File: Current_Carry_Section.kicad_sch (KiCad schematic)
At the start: 4 parts, among them U3_1 TPS259620DDAR, U3_2 TPS259620DDAR, U3_3 TPS259620DDAR, U3_4 TPS259620DDAR

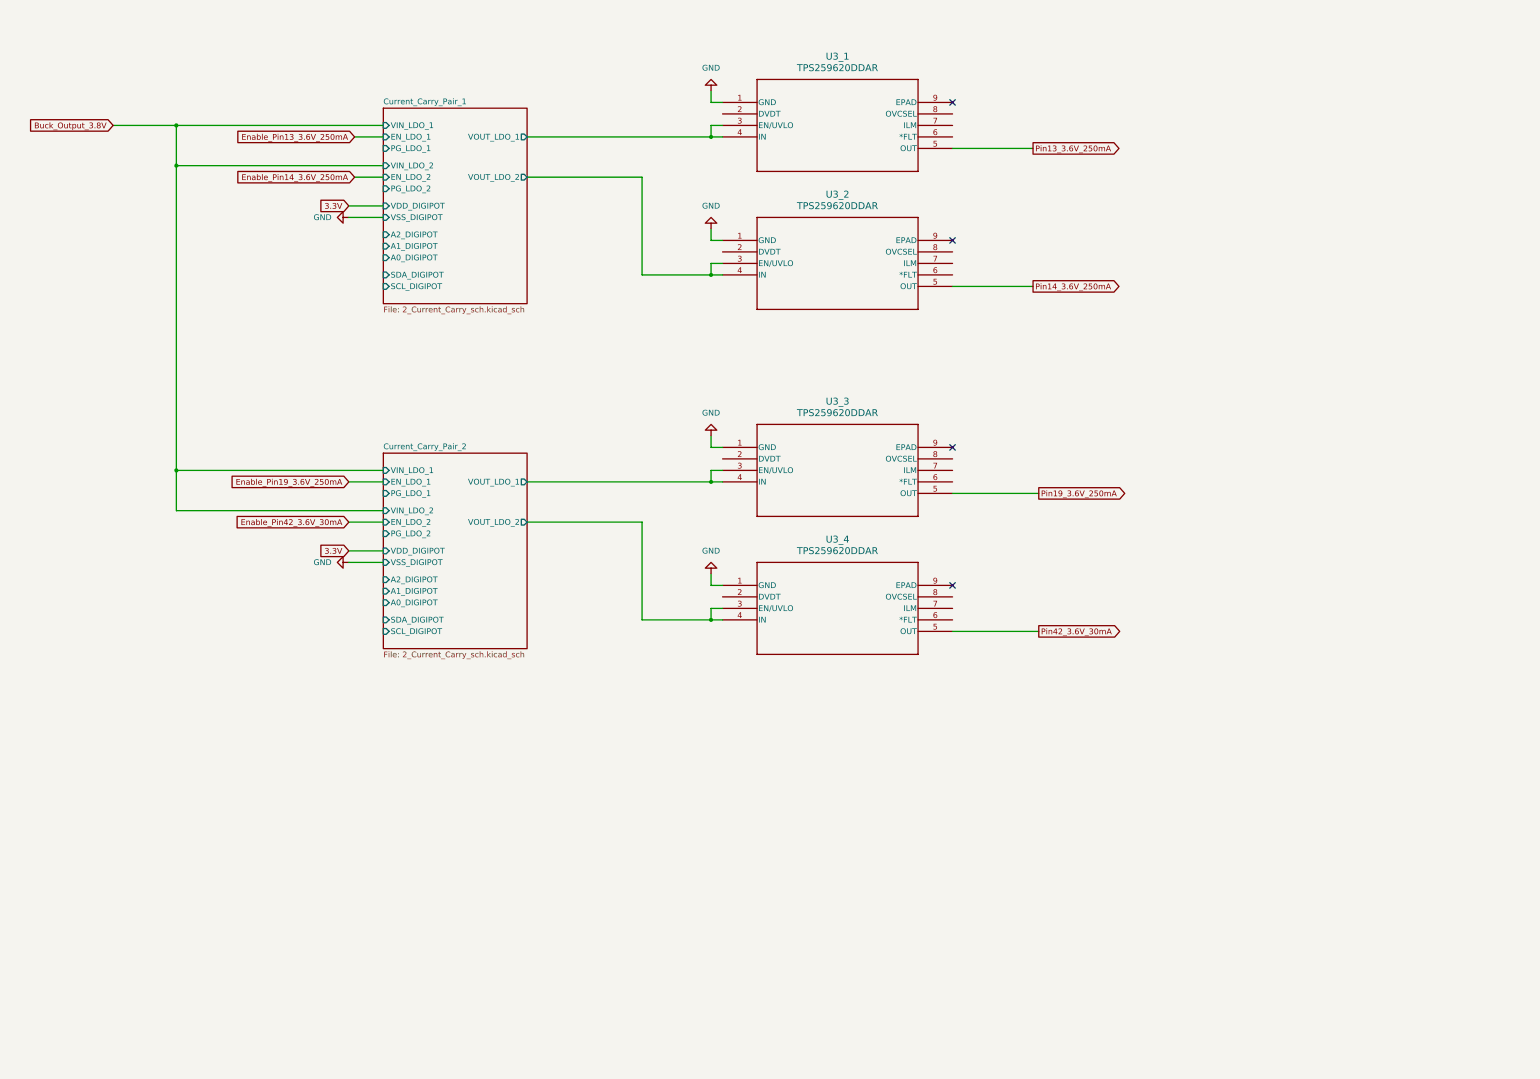
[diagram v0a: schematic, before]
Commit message: Full schematic connection without ratio consideration.
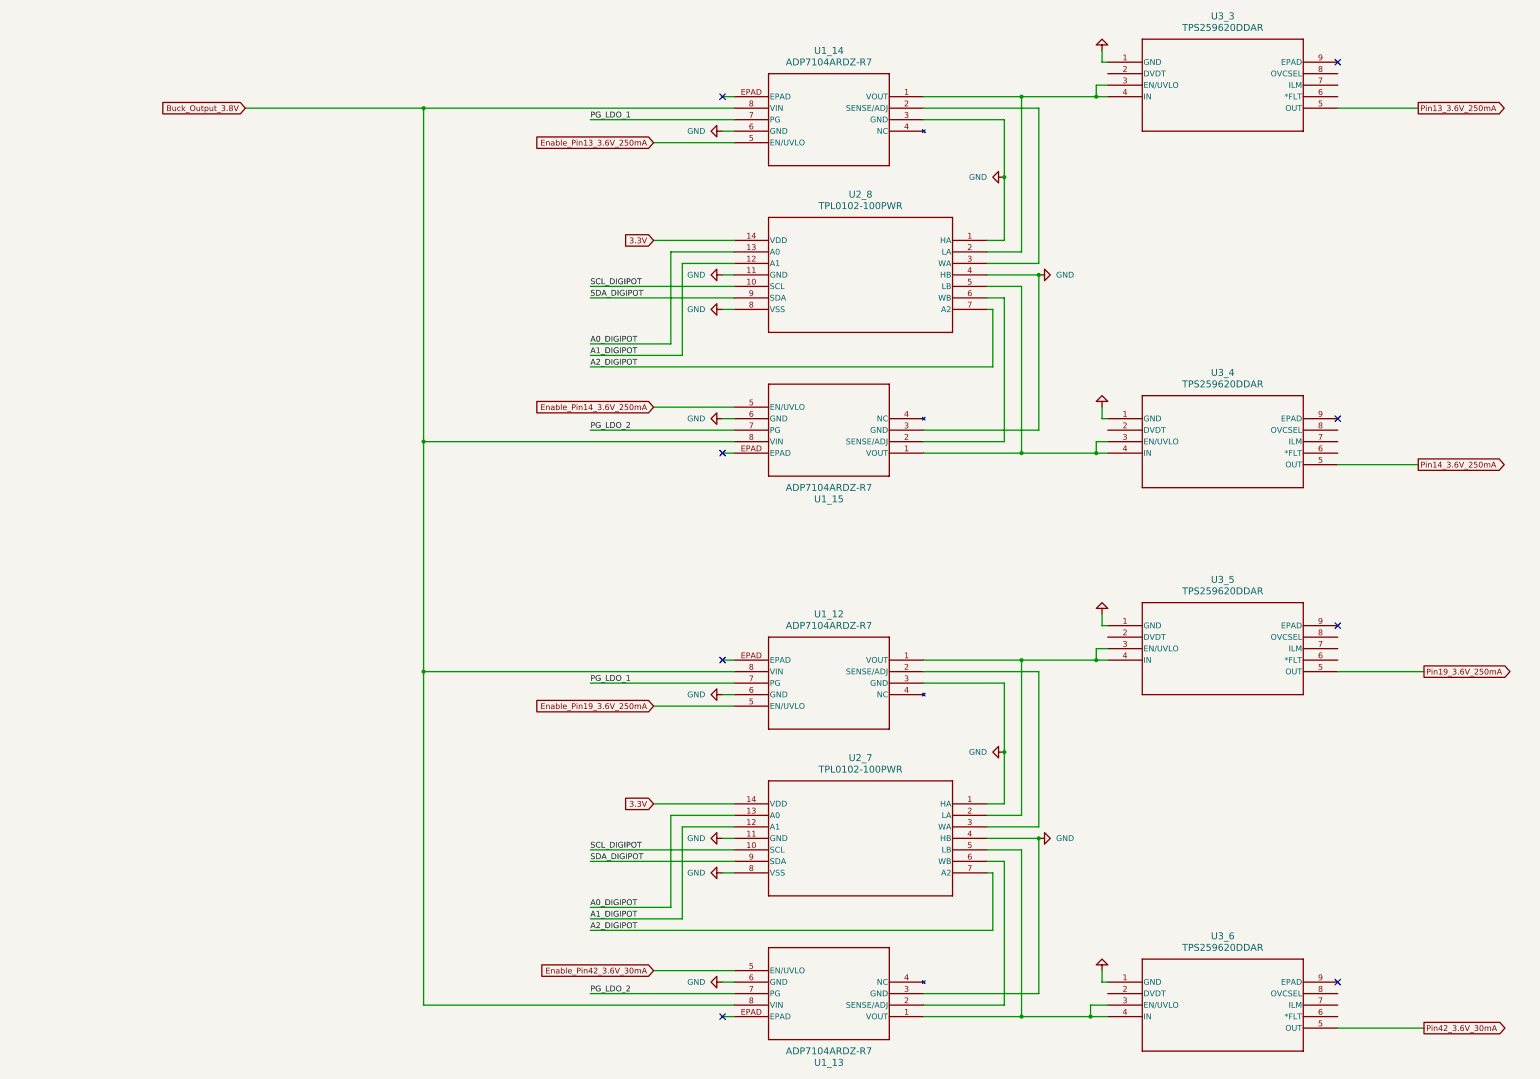
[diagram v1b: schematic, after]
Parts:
- added U1_12, U1_13, U1_14, U1_15: ADP7104ARDZ-R7, RD_8_2_ADI, symbol Adjustable Low-Dropout Regulator:ADP7104ARDZ-R7
- added U2_7, U2_8: TPL0102-100PWR, PW14, symbol Digital Potentiometer:TPL0102-100PWR
- renumbered U3_1 to U3_3, U3_2 to U3_4, U3_3 to U3_5, U3_4 to U3_6
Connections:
- net 3.3V: now also U2_7.14 (VDD), U2_8.14 (VDD)
- net Buck_Output_3.8V: now also U1_12.8 (VIN), U1_13.8 (VIN), U1_14.8 (VIN), U1_15.8 (VIN)
- net Enable_Pin13_3.6V_250mA: now also U1_14.5 (EN/UVLO)
- net Enable_Pin14_3.6V_250mA: now also U1_15.5 (EN/UVLO)
- net Enable_Pin19_3.6V_250mA: now also U1_12.5 (EN/UVLO)
- net Enable_Pin42_3.6V_30mA: now also U1_13.5 (EN/UVLO)
- net GND: now also U1_12.3 (GND), U1_12.6 (GND), U1_13.3 (GND), U1_13.6 (GND), U1_14.3 (GND), U1_14.6 (GND), U1_15.3 (GND), U1_15.6 (GND), U2_7.1 (HA), U2_7.11 (GND), U2_7.4 (HB), U2_7.8 (VSS), U2_8.1 (HA), U2_8.11 (GND), U2_8.4 (HB), U2_8.8 (VSS)
- net Current_Carry_Pair_1/VOUT_LDO_1: no longer names the net of U3_3.3 (EN/UVLO), U3_3.4 (IN)
- net Current_Carry_Pair_1/VOUT_LDO_1: now also U1_14.1 (VOUT), U2_8.2 (LA)
- net Current_Carry_Pair_1/VOUT_LDO_2: no longer names the net of U3_4.3 (EN/UVLO), U3_4.4 (IN)
- net Current_Carry_Pair_1/VOUT_LDO_2: now also U1_15.1 (VOUT), U2_8.5 (LB)
- net Current_Carry_Pair_2/VOUT_LDO_1: no longer names the net of U3_5.3 (EN/UVLO), U3_5.4 (IN)
- net Current_Carry_Pair_2/VOUT_LDO_1: now also U1_12.1 (VOUT), U2_7.2 (LA)
- net Current_Carry_Pair_2/VOUT_LDO_2: no longer names the net of U3_6.3 (EN/UVLO), U3_6.4 (IN)
- net Current_Carry_Pair_2/VOUT_LDO_2: now also U1_13.1 (VOUT), U2_7.5 (LB)
- new net: U1_12.2 (SENSE/ADJ), U2_7.3 (WA)
- new net: U1_13.2 (SENSE/ADJ), U2_7.6 (WB)
- new net: U1_14.2 (SENSE/ADJ), U2_8.3 (WA)
- new net: U1_15.2 (SENSE/ADJ), U2_8.6 (WB)
- new net A0_DIGIPOT: U2_7.13 (A0), U2_8.13 (A0)
- new net A1_DIGIPOT: U2_7.12 (A1), U2_8.12 (A1)
- new net A2_DIGIPOT: U2_7.7 (A2), U2_8.7 (A2)
- new net PG_LDO_1: U1_12.7 (PG), U1_14.7 (PG)
- new net PG_LDO_2: U1_13.7 (PG), U1_15.7 (PG)
- new net SCL_DIGIPOT: U2_7.10 (SCL), U2_8.10 (SCL)
- new net SDA_DIGIPOT: U2_7.9 (SDA), U2_8.9 (SDA)
- no-connect marks 4 -> 8
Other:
- removed sheet Current_Carry_Pair_1
- removed sheet Current_Carry_Pair_2
- moved on the sheet: U3_3, U3_4, U3_5, U3_6
